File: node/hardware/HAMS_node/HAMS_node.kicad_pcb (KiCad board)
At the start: 2 copper layers, 47.5 x 50 mm, 45 parts, among them J1 Conn_01x02, J2 Conn_02x07_Odd_Even, J3 Conn_01x08, J4 Conn_01x04, J5 Conn_01x04, J6 Conn_01x04, J7 Conn_01x04, Q1 DMP3099L, SW1 TL3305BF100QG, SW2 JS202011SCQN, U1 NRF24L01_Breakout, U2 nRF24L01p SMD module, U3 STM32L031K6Tx, Y1 CM9V-T1A

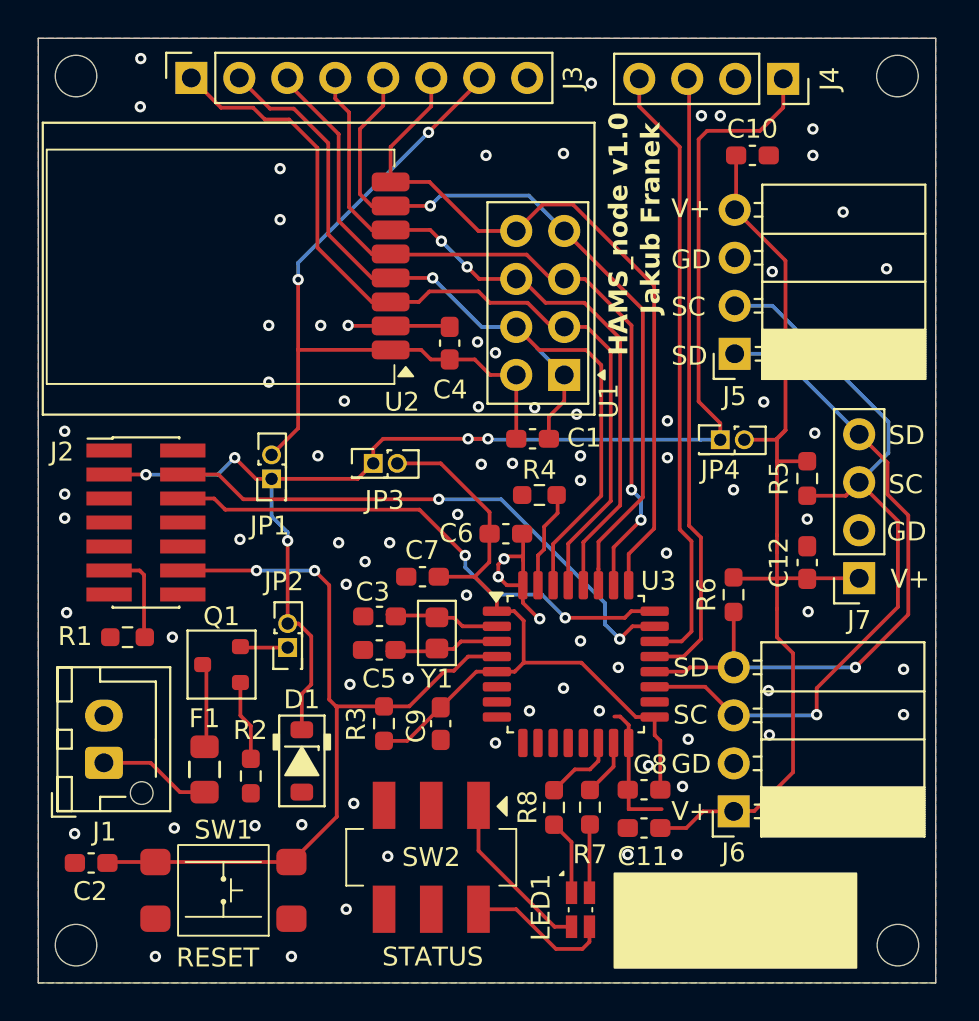
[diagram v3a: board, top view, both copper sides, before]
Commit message: Improve HAMS node HW: schematic and PCB
Add UART support to the ST-LINK programmer header.
Update task list.
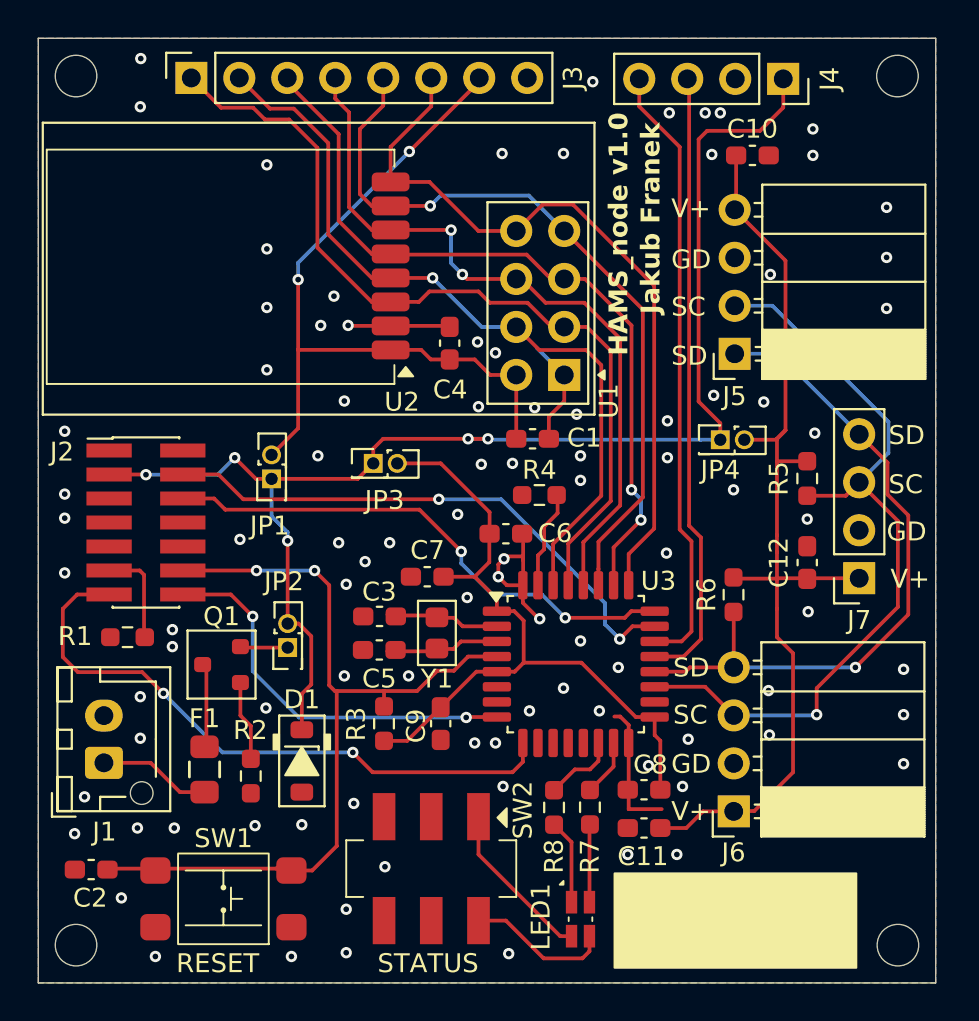
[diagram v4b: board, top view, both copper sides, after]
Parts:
- moved SW2 0.60 mm to (187.4, 101.5)
- moved LED1 0.50 mm to (195.3, 104.1)
- moved SW1 0.45 mm to (176.4, 103.2)
- moved C2 0.35 mm to (169.4, 101.6)
- moved C7 0.25 mm to (187.2, 86.1)
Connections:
- J2 pad 13: unconnected-(J2-Pin_13-Pad13) -> /VCP_RX
- J2 pad 14: unconnected-(J2-Pin_14-Pad14) -> /VCP_TX
- U3 pad 8: unconnected-(U3-PA2-Pad8) -> /VCP_TX
- U3 pad 9: unconnected-(U3-PA3-Pad9) -> /VCP_RX
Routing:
- net /VCP_RX: track 0.00 -> 33.4 mm, vias 0 -> 2
- net /VCP_TX: track 0.00 -> 21.0 mm, vias 0 -> 2
- net /NRST: track 43.0 -> 44.5 mm
- net /SPI_MOSI: track 38.3 -> 39.3 mm
- net GND: vias 78 -> 95
